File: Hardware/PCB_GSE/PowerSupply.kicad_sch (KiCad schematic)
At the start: 64 parts, among them J8 Vin_XT30PW-F, U1 L6981N33DR, U3 MPQ9843GLE-5-AEC1-Z, U7 LM2673SX-12_NOPB

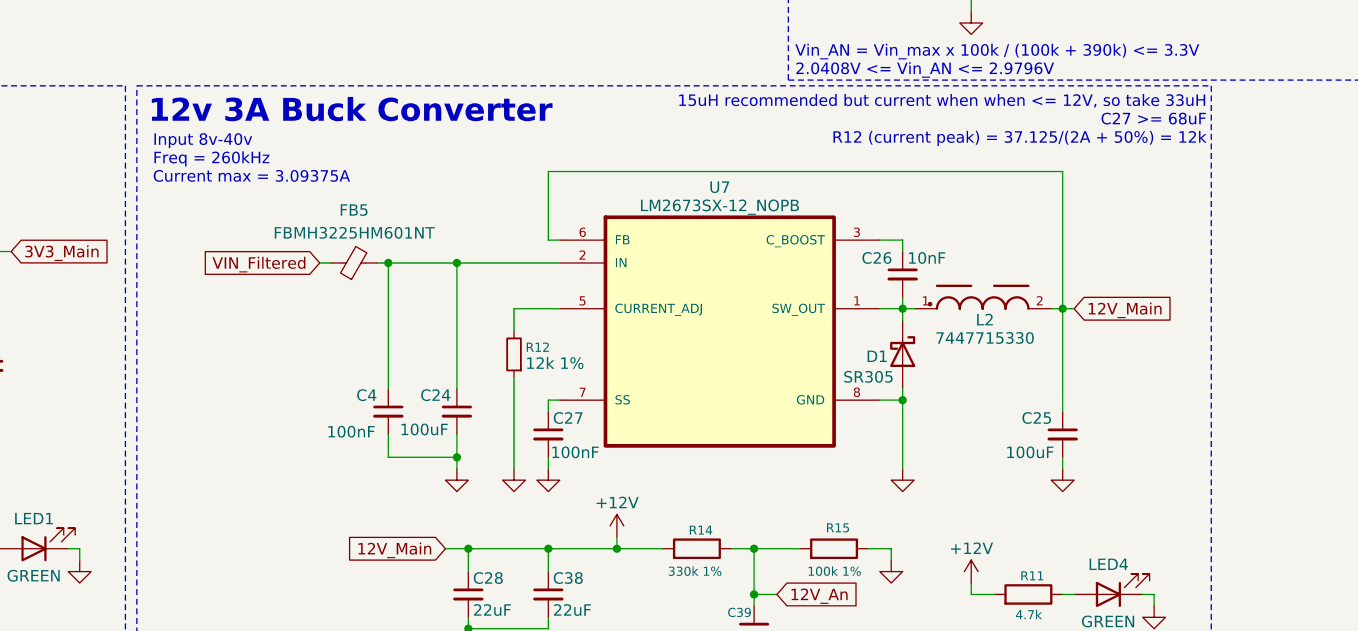
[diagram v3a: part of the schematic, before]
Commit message: fix: stm32 project + modified 12v buck symbol
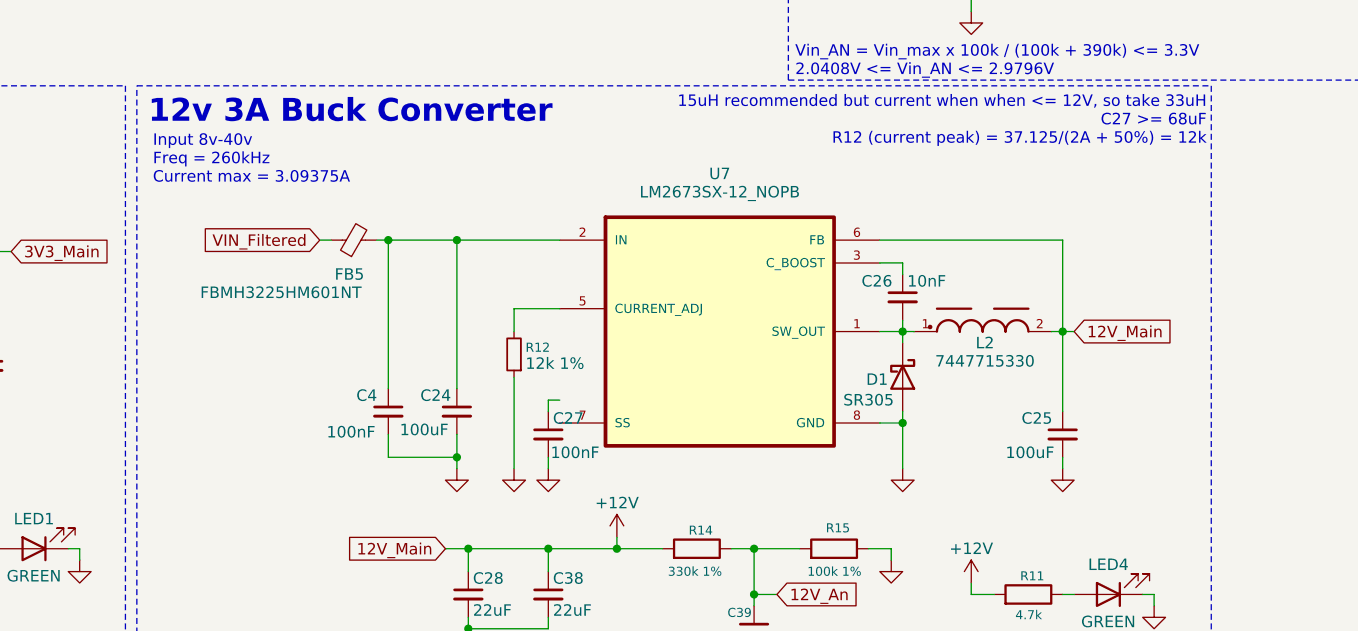
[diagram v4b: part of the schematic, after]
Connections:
- net at C27.1: no longer U7.7 (SS)
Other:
- moved on the sheet: C26, D1, FB5, L2

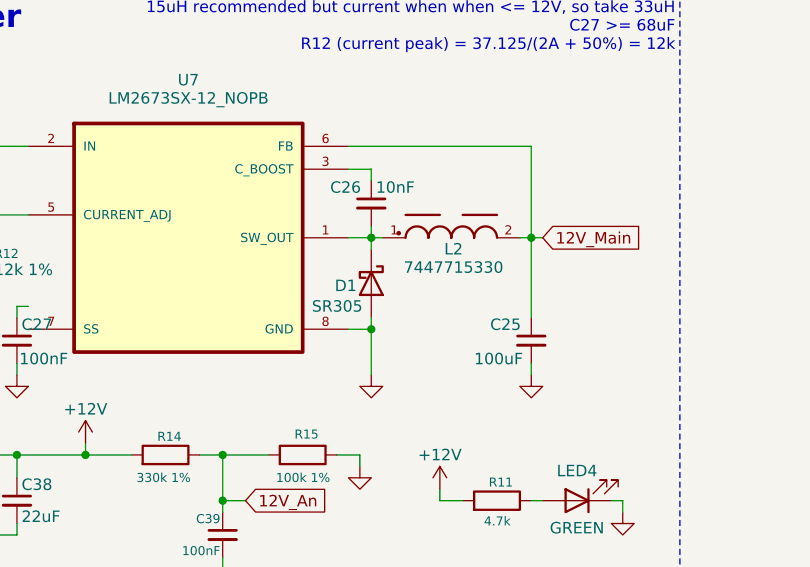
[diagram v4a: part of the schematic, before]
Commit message: fix: change Schottky diode 12v buck
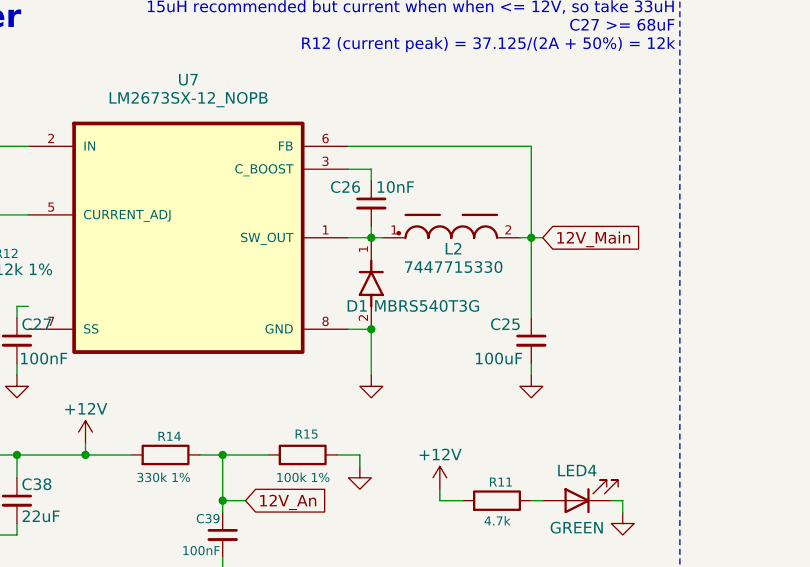
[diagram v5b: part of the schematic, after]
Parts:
- removed D1: SR305, symbol Device:D_Schottky
- added D1: MBRS540T3G, MBRS540T3G:DIOM7959X261N, symbol PCB_GSE:MBRS540T3G
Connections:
- net AGND5V: now also D1.2
- net at C26.2, L2.1, U7.1 (SW_OUT): now also D1.1
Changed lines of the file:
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@@
 	)
 	(junction
+		(at 219.71 88.9)
+		(diameter 0)
+		(color 0 0 0 0)
+	)
+	(junction
 		(at 58.42 144.78)
 		(diameter 0)
@@
 	)
 	(junction
-		(at 219.71 88.9)
-		(diameter 0)
-		(color 0 0 0 0)
-	)
-	(junction
 		(at 46.99 88.9)
 		(diameter 0)
@@
 	(wire
 		(pts
-			(xy 208.28 102.87) (xy 203.2 102.87)
+			(xy 217.17 88.9) (xy 219.71 88.9)
 		)
 		(stroke
@@
 	(wire
 		(pts
-			(xy 227.33 43.18) (xy 227.33 41.91)
+			(xy 208.28 102.87) (xy 203.2 102.87)
 		)
 		(stroke
@@
 	(wire
 		(pts
-			(xy 77.47 144.78) (xy 80.01 144.78)
+			(xy 227.33 43.18) (xy 227.33 41.91)
 		)
 		(stroke
@@
 	(wire
 		(pts
-			(xy 48.26 153.67) (xy 39.37 153.67)
+			(xy 77.47 144.78) (xy 80.01 144.78)
 		)
 		(stroke
@@
 	(wire
 		(pts
-			(xy 161.29 168.91) (xy 161.29 166.37)
+			(xy 48.26 153.67) (xy 39.37 153.67)
 		)
 		(stroke
@@
 	(wire
 		(pts
-			(xy 39.37 69.85) (xy 46.99 69.85)
+			(xy 161.29 168.91) (xy 161.29 166.37)
 		)
 		(stroke
@@
 	(wire
 		(pts
-			(xy 162.56 92.71) (xy 162.56 90.17)
+			(xy 39.37 69.85) (xy 46.99 69.85)
 		)
 		(stroke
@@
 	(wire
 		(pts
-			(xy 87.63 64.77) (xy 91.44 64.77)
+			(xy 162.56 92.71) (xy 162.56 90.17)
 		)
 		(stroke
@@
 	(wire
 		(pts
-			(xy 219.71 80.01) (xy 219.71 78.74)
+			(xy 87.63 64.77) (xy 91.44 64.77)
 		)
 		(stroke
@@
 	(wire
 		(pts
-			(xy 219.71 87.63) (xy 219.71 88.9)
-		)
-		(stroke
-			(width 0)
-			(type default)
-		)
-	)
-	(wire
-		(pts
 			(xy 49.53 111.76) (xy 49.53 113.03)
 		)
@@
 	(wire
 		(pts
-			(xy 219.71 88.9) (xy 217.17 88.9)
-		)
-		(stroke
-			(width 0)
-			(type default)
-		)
-	)
-	(wire
-		(pts
 			(xy 170.18 92.71) (xy 170.18 93.98)
 		)
@@
 	)
 	(symbol
-		(lib_id "Device:D_Schottky")
-		(at 219.71 83.82 270)
-		(unit 1)
-		(exclude_from_sim no)
-		(in_bom yes)
-		(on_board yes)
-		(dnp no)
-		(property "Reference" "D1"
-			(at 215.646 84.074 90)
-			(effects
-				(font
-					(size 1.27 1.27)
-				)
-				(justify left)
-			)
-		)
-		(property "Value" "SR305"
-			(at 213.106 86.36 90)
-			(effects
-				(font
-					(size 1.27 1.27)
-				)
-				(justify left)
-			)
-		)
-		(property "Footprint" ""
-			(at 219.71 83.82 0)
-			(effects
-				(font
-					(size 1.27 1.27)
-				)
-				(hide yes)
-			)
-		)
-		(property "Datasheet" "~"
-			(at 219.71 83.82 0)
-			(effects
-				(font
-					(size 1.27 1.27)
-				)
-				(hide yes)
-			)
-		)
-		(property "Description" "Schottky diode"
-			(at 219.71 83.82 0)
-			(effects
-				(font
-					(size 1.27 1.27)
-				)
-				(hide yes)
-			)
-		)
-		(pin "1"
-		)
-		(pin "2"
-		)
-		(instances
-			(project ""
-				(path "/a63f9ed4-21e4-42d0-8bfc-f96143f84d4d/8a1a8d24-b3b8-4669-940a-297f990b7d99"
-					(reference "D1")
-					(unit 1)
-				)
-			)
-		)
-	)
-	(symbol
 		(lib_id "power:+3V3")
 		(at 71.12 134.62 0)
@@
 					(unit 1)
 				)
+			)
+		)
+	)
+	(symbol
+		(lib_id "PCB_GSE:MBRS540T3G")
+		(at 219.71 83.82 90)
+		(unit 1)
+		(exclude_from_sim no)
+		(in_bom yes)
+		(on_board yes)
+		(dnp no)
+		(property "Reference" "D1"
+			(at 216.916 86.36 90)
+			(effects
+				(font
+					(size 1.27 1.27)
+				)
+				(justify right)
+			)
+		)
+		(property "Value" "MBRS540T3G"
+			(at 219.964 86.36 90)
+			(effects
+				(font
+					(size 1.27 1.27)
+				)
+				(justify right)
+			)
+		)
+		(property "Footprint" "MBRS540T3G:DIOM7959X261N"
+			(at 213.868 70.358 0)
+			(effects
+				(font
+					(size 1.27 1.27)
+				)
+				(justify bottom)
+				(hide yes)
+			)
+		)
+		(property "Datasheet" ""
+			(at 219.71 83.82 0)
+			(effects
+				(font
+					(size 1.27 1.27)
+				)
+				(hide yes)
+			)
+		)
+		(property "Description" ""
+			(at 219.71 83.82 0)
+			(effects
+				(font
+					(size 1.27 1.27)
+				)
+				(hide yes)
+			)
+		)
+		(property "DigiKey_Part_Number" "MBRS540T3GOSCT-ND"
+			(at 214.376 73.406 0)
+			(effects
+				(font
+					(size 1.27 1.27)
+				)
+				(justify bottom)
+				(hide yes)
+			)
+		)
+		(property "SnapEDA_Link" "https://www.snapeda.com/parts/MBRS540T3G/Onsemi/view-part/?ref=snap"
+			(at 213.36 67.056 0)
+			(effects
+				(font
+					(size 1.27 1.27)
+				)
+				(justify bottom)
+				(hide yes)
+			)
+		)
+		(property "MAXIMUM_PACKAGE_HEIGHT" "2.61 mm"
+			(at 210.82 83.566 0)
+			(effects
+				(font
+					(size 1.27 1.27)
+				)
+				(justify bottom)
+				(hide yes)
+			)
+		)
+		(property "Package" "SMC-2 ON Semiconductor"
+			(at 214.376 72.644 0)
+			(effects
+				(font
+					(size 1.27 1.27)
+				)
+				(justify bottom)
+				(hide yes)
+			)
+		)
+		(property "Check_prices" "https://www.snapeda.com/parts/MBRS540T3G/Onsemi/view-part/?ref=eda"
+			(at 213.868 66.548 0)
+			(effects
+				(font
+					(size 1.27 1.27)
+				)
+				(justify bottom)
+				(hide yes)
+			)
+		)
+		(property "STANDARD" "IPC-7351B"
+			(at 212.09 83.312 0)
+			(effects
+				(font
+					(size 1.27 1.27)
+				)
+				(justify bottom)
+				(hide yes)
+			)
+		)
+		(property "PARTREV" "7/27/2017"
+			(at 211.836 83.312 0)
+			(effects
+				(font
+					(size 1.27 1.27)
+				)
+				(justify bottom)
+				(hide yes)
+			)
+		)
+		(property "MF" "ON Semiconductor"
+			(at 208.026 91.948 0)
+			(effects
+				(font
+					(size 1.27 1.27)
+				)
+				(justify bottom)
+				(hide yes)
+			)
+		)
+		(property "MP" "MBRS540T3G"
+			(at 211.582 83.312 0)
+			(effects
+				(font
+					(size 1.27 1.27)
+				)
+				(justify bottom)
+				(hide yes)
+			)
+		)
+		(property "Description_1" "Diode Schottky 40 V 5A Surface Mount SMC"
+			(at 213.868 69.088 0)
+			(effects
+				(font
+					(size 1.27 1.27)
+				)
+				(justify bottom)
+				(hide yes)
+			)
+		)
+		(property "MANUFACTURER" "ON SEMICONDUCTOR"
+			(at 209.804 84.074 0)
+			(effects
+				(font
+					(size 1.27 1.27)
+				)
+				(justify bottom)
+				(hide yes)
+			)
+		)
+		(pin "2"
+		)
+		(pin "1"
+		)
+		(instances
+			(project ""
+				(path "/a63f9ed4-21e4-42d0-8bfc-f96143f84d4d/8a1a8d24-b3b8-4669-940a-297f990b7d99"
+					(reference "D1")
+					(unit 1)
+				)
